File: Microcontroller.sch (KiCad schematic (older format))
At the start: 27 parts

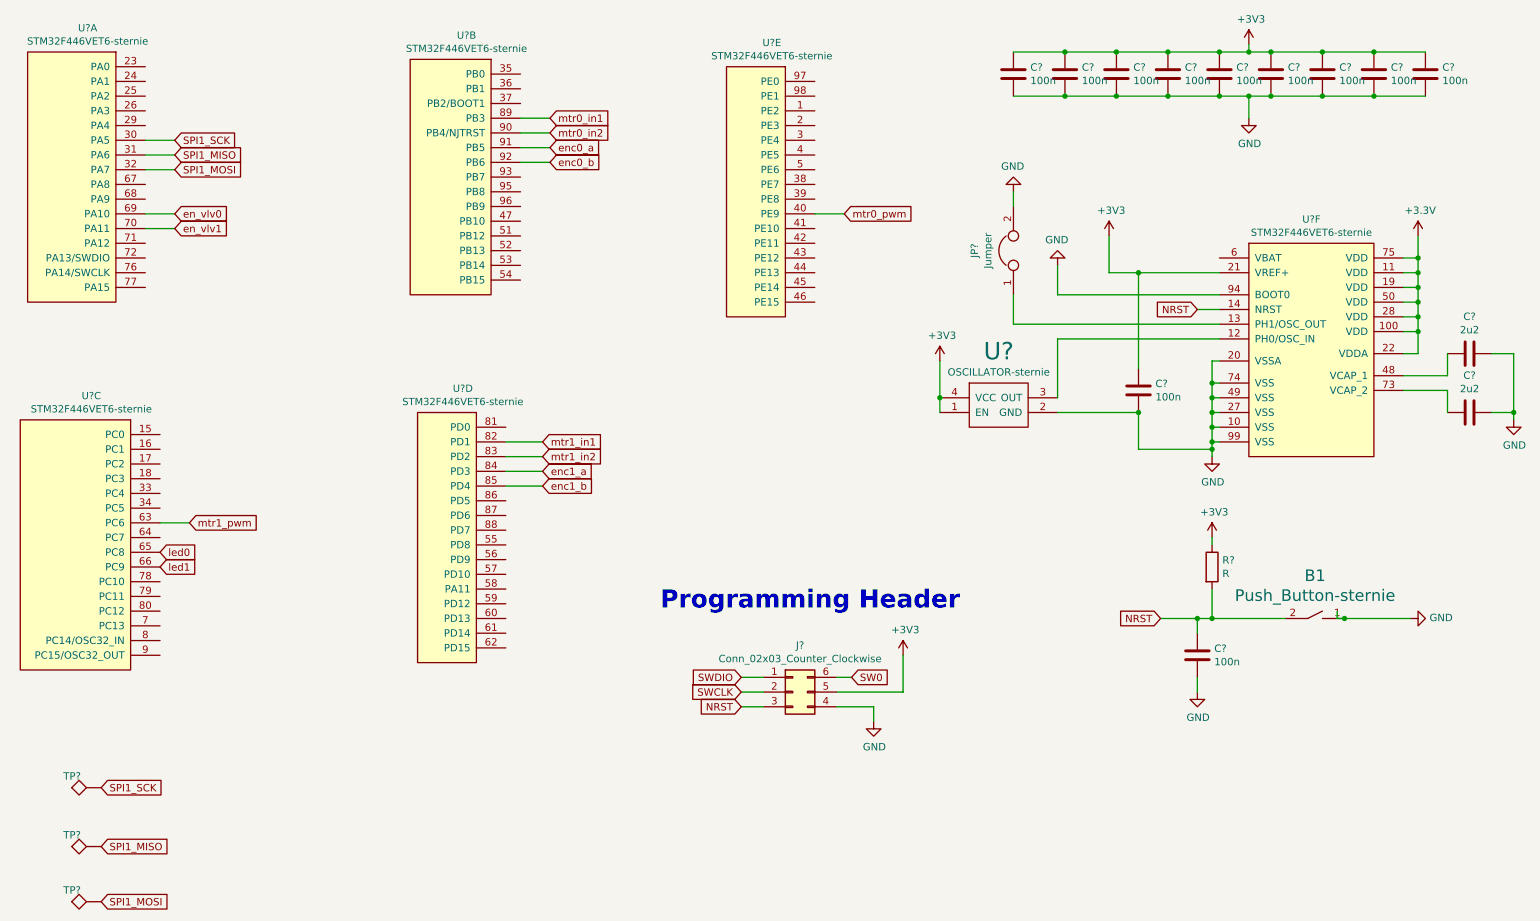
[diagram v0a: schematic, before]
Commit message: Eletrical Rules Check
Fixed some label names
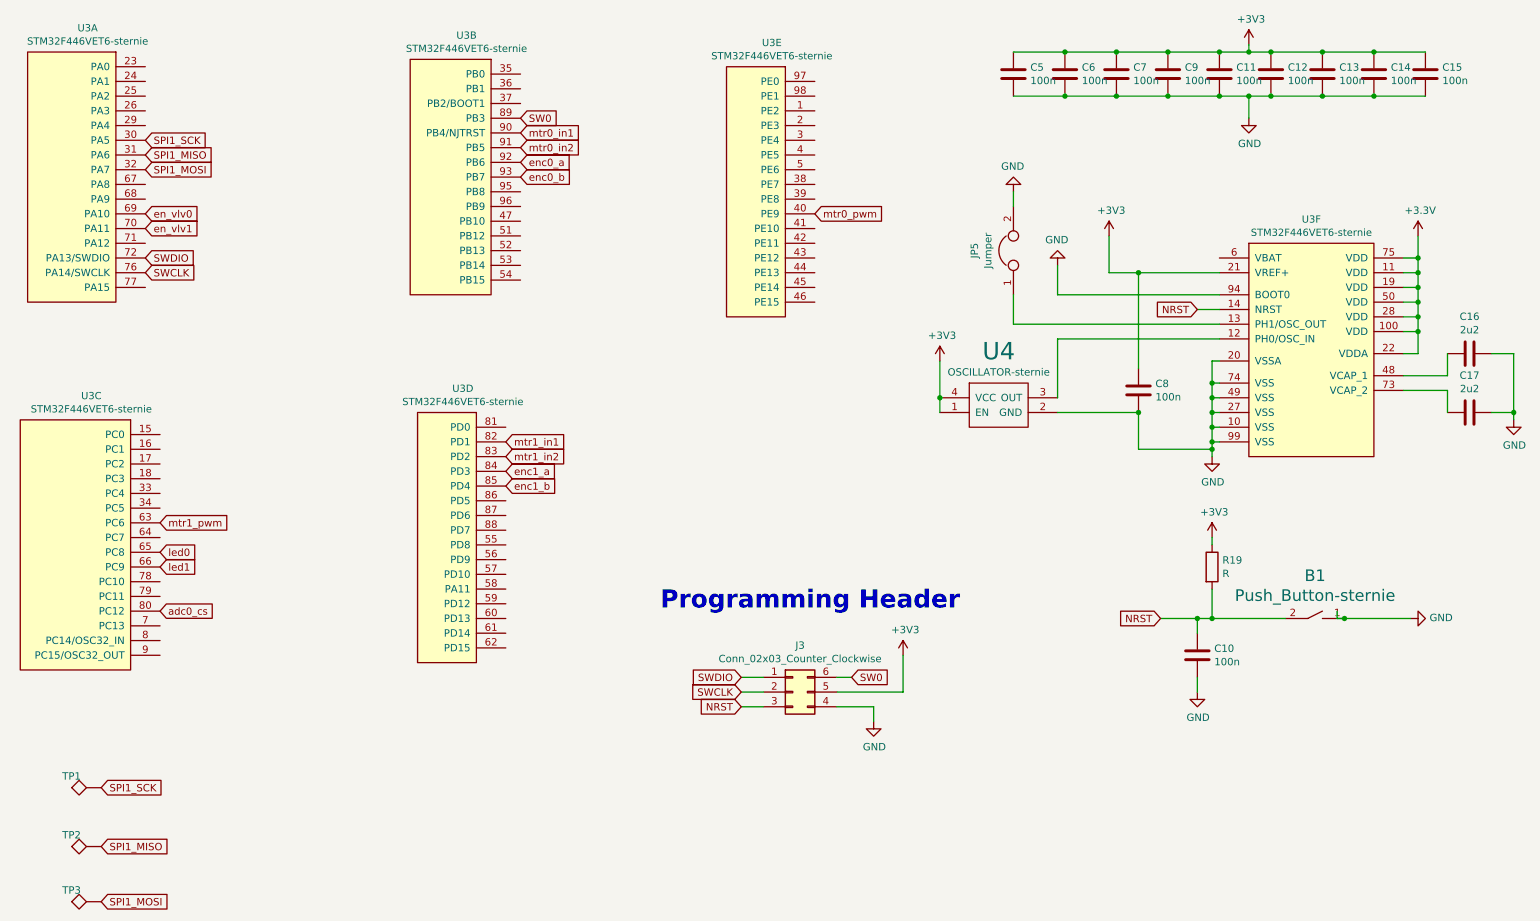
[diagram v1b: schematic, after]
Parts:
- gave numbers to parts that had none: 21
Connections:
- net SW0: now also U3.89 (PB3)
- net SWCLK: now also U3.76 (PA14/SWCLK)
- net SWDIO: now also U3.72 (PA13/SWDIO)
- net enc0_a: now also U3.92 (PB6); no longer U3.91 (PB5)
- net enc0_b: now also U3.93 (PB7); no longer U3.92 (PB6)
- net mtr0_in1: now also U3.90 (PB4/NJTRST); no longer U3.89 (PB3)
- net mtr0_in2: now also U3.91 (PB5); no longer U3.90 (PB4/NJTRST)
- net adc0_cs: now reaches U3.80 (PC12)
